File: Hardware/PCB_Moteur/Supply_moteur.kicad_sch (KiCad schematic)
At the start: 26 parts, among them J1 XT30PW-F, U1 L6981N33DR

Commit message: wip: arrangement connecteurs et modeles 3D
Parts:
- L2: DigiKey_Part_Number (none) -> 732-2196-1-ND
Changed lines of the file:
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@@
 			)
 		)
-		(property "Datasheet" ""
+		(property "Datasheet" "https://www.we-online.com/components/products/datasheet/7447715330.pdf"
 			(at 106.68 81.28 0)
 			(effects
@@
 			(at 106.68 81.28 0)
 			(effects
+				(font
+					(size 1.27 1.27)
+				)
+				(hide yes)
+			)
+		)
+		(property "DigiKey_Part_Number" "732-2196-1-ND"
+			(at 106.68 81.28 0)
+			(effects

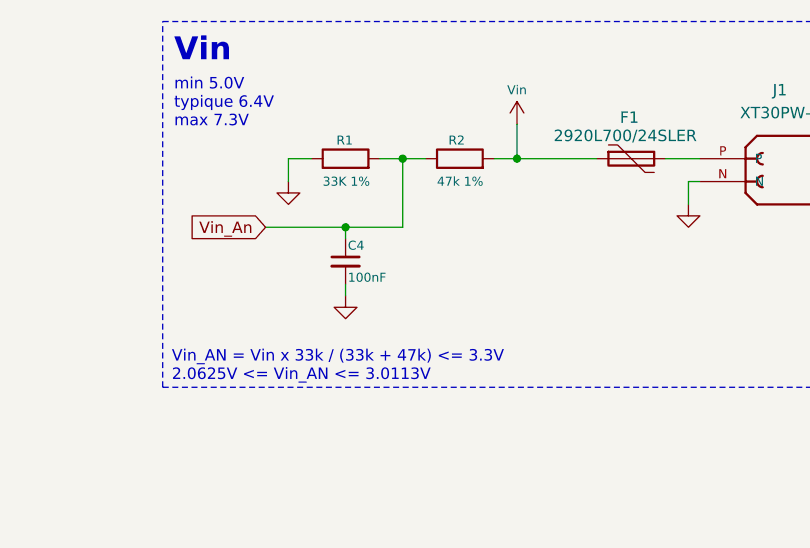
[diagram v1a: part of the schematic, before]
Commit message: fix(GSE & Moteur): change Vin adc divider
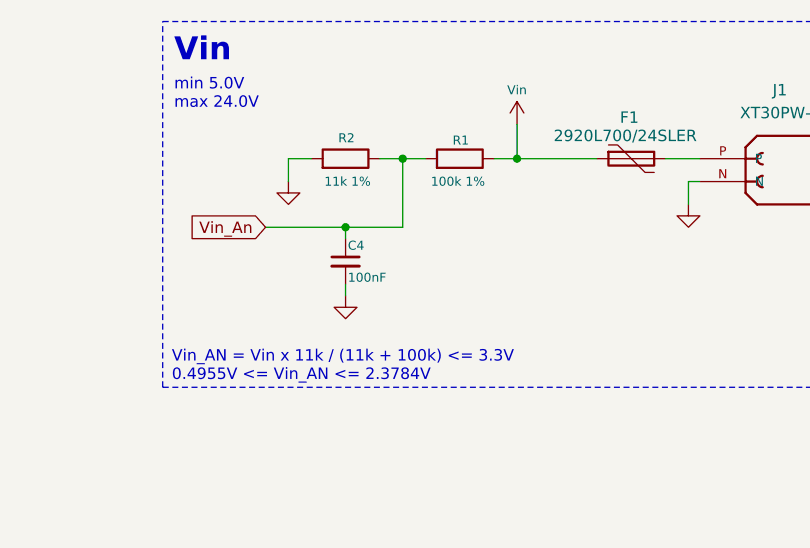
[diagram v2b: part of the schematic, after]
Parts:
- R1: value 33K 1% -> 100k 1%
- R2: value 47k 1% -> 11k 1%
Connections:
- net GND: now also R2.2; no longer R1.1
- net Vin: now also R1.1; no longer R2.2
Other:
- note added: "Vin_AN = Vin x 11k / (11k + 100k) <= 3.3V 0.4955V <= Vin_AN <= 2.3784V"
- note added: "min 5.0V max 24.0V"
- note removed: "Vin_AN = Vin x 33k / (33k + 47k) <= 3.3V 2.0625V <= Vin_AN <= 3.0113V"
- note removed: "min 5.0V typique 6.4V max 7.3V"
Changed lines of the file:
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@@
 		)
 	)
-	(text "Vin_AN = Vin x 33k / (33k + 47k) <= 3.3V\n2.0625V <= Vin_AN <= 3.0113V"
+	(text "Vin_AN = Vin x 11k / (11k + 100k) <= 3.3V\n0.4955V <= Vin_AN <= 2.3784V"
 		(exclude_from_sim no)
 		(at 208.026 51.054 0)
@@
 		)
 	)
-	(text "min 5.0V\ntypique 6.4V\nmax 7.3V"
+	(text "min 5.0V\nmax 24.0V"
 		(exclude_from_sim no)
 		(at 208.28 19.05 0)
@@
 	)
 	(symbol
+		(lib_id "Device:R")
+		(at 227.33 27.94 270)
+		(mirror x)
+		(unit 1)
+		(exclude_from_sim no)
+		(in_bom yes)
+		(on_board yes)
+		(dnp no)
+		(property "Reference" "R2"
+			(at 228.346 25.654 90)
+			(effects
+				(font
+					(size 1 1)
+				)
+				(justify right)
+			)
+		)
+		(property "Value" "11k 1%"
+			(at 230.124 30.48 90)
+			(effects
+				(font
+					(size 1 1)
+				)
+				(justify right)
+			)
+		)
+		(property "Footprint" "Resistor_SMD:R_0805_2012Metric"
+			(at 227.33 29.718 90)
+			(effects
+				(font
+					(size 1 1)
+				)
+				(hide yes)
+			)
+		)
+		(property "Datasheet" "~"
+			(at 227.33 27.94 0)
+			(effects
+				(font
+					(size 1 1)
+				)
+				(hide yes)
+			)
+		)
+		(property "Description" ""
+			(at 227.33 27.94 0)
+			(effects
+				(font
+					(size 1.27 1.27)
+				)
+				(hide yes)
+			)
+		)
+		(pin "1"
+		)
+		(pin "2"
+		)
+		(instances
+			(project "PCB_moteur"
+				(path "/b0d87684-7b1c-41d8-8358-755aa327573e/92d1df5d-a307-4eea-a65c-ade4cb0ad548"
+					(reference "R2")
+					(unit 1)
+				)
+			)
+		)
+	)
+	(symbol
 		(lib_id "Device:LED")
 		(at 123.19 109.22 180)
@@
 	)
 	(symbol
-		(lib_id "Device:R")
-		(at 227.33 27.94 90)
-		(unit 1)
-		(exclude_from_sim no)
-		(in_bom yes)
-		(on_board yes)
-		(dnp no)
-		(property "Reference" "R1"
-			(at 226.314 25.908 90)
-			(effects
-				(font
-					(size 1 1)
-				)
-				(justify right)
-			)
-		)
-		(property "Value" "33K 1%"
-			(at 224.79 30.48 90)
-			(effects
-				(font
-					(size 1 1)
-				)
-				(justify right)
-			)
-		)
-		(property "Footprint" "Resistor_SMD:R_0805_2012Metric"
-			(at 227.33 29.718 90)
-			(effects
-				(font
-					(size 1 1)
-				)
-				(hide yes)
-			)
-		)
-		(property "Datasheet" "~"
-			(at 227.33 27.94 0)
-			(effects
-				(font
-					(size 1 1)
-				)
-				(hide yes)
-			)
-		)
-		(property "Description" ""
-			(at 227.33 27.94 0)
-			(effects
-				(font
-					(size 1.27 1.27)
-				)
-				(hide yes)
-			)
-		)
-		(pin "1"
-		)
-		(pin "2"
-		)
-		(instances
-			(project "PCB_moteur"
-				(path "/b0d87684-7b1c-41d8-8358-755aa327573e/92d1df5d-a307-4eea-a65c-ade4cb0ad548"
-					(reference "R1")
-					(unit 1)
-				)
-			)
-		)
-	)
-	(symbol
 		(lib_id "Device:C_Small")
 		(at 40.64 115.57 0)
@@
 	)
 	(symbol
-		(lib_id "Device:R")
-		(at 240.03 27.94 90)
-		(unit 1)
-		(exclude_from_sim no)
-		(in_bom yes)
-		(on_board yes)
-		(dnp no)
-		(property "Reference" "R2"
-			(at 238.76 25.908 90)
-			(effects
-				(font
-					(size 1 1)
-				)
-				(justify right)
-			)
-		)
-		(property "Value" "47k 1%"
-			(at 237.49 30.48 90)
-			(effects
-				(font
-					(size 1 1)
-				)
-				(justify right)
-			)
-		)
-		(property "Footprint" "Resistor_SMD:R_0805_2012Metric"
-			(at 240.03 29.718 90)
-			(effects
-				(font
-					(size 1 1)
-				)
-				(hide yes)
-			)
-		)
-		(property "Datasheet" "~"
-			(at 240.03 27.94 0)
-			(effects
-				(font
-					(size 1 1)
-				)
-				(hide yes)
-			)
-		)
-		(property "Description" ""
-			(at 240.03 27.94 0)
-			(effects
-				(font
-					(size 1.27 1.27)
-				)
-				(hide yes)
-			)
-		)
-		(pin "1"
-		)
-		(pin "2"
-		)
-		(instances
-			(project "PCB_moteur"
-				(path "/b0d87684-7b1c-41d8-8358-755aa327573e/92d1df5d-a307-4eea-a65c-ade4cb0ad548"
-					(reference "R2")
-					(unit 1)
-				)
-			)
-		)
-	)
-	(symbol
 		(lib_id "power:GND")
 		(at 220.98 30.48 0)
@@
 					(unit 1)
 				)
+			)
+		)
+	)
+	(symbol
+		(lib_id "Device:R")
+		(at 240.03 27.94 270)
+		(mirror x)
+		(unit 1)
+		(exclude_from_sim no)
+		(in_bom yes)
+		(on_board yes)
+		(dnp no)
+		(property "Reference" "R1"
+			(at 241.046 25.908 90)
+			(effects
+				(font
+					(size 1 1)
+				)
+				(justify right)
+			)
+		)
+		(property "Value" "100k 1%"
+			(at 242.824 30.48 90)
+			(effects
+				(font
+					(size 1 1)
+				)
+				(justify right)
+			)
+		)
+		(property "Footprint" "Resistor_SMD:R_0805_2012Metric"
+			(at 240.03 29.718 90)
+			(effects
+				(font
+					(size 1 1)
+				)
+				(hide yes)
+			)
+		)
+		(property "Datasheet" "~"
+			(at 240.03 27.94 0)
+			(effects
+				(font
+					(size 1 1)
+				)
+				(hide yes)
+			)
+		)
+		(property "Description" ""
+			(at 240.03 27.94 0)
+			(effects
+				(font
+					(size 1.27 1.27)
+				)
+				(hide yes)
+			)
+		)
+		(pin "1"
+		)
+		(pin "2"
+		)
+		(instances
+			(project "PCB_moteur"
+				(path "/b0d87684-7b1c-41d8-8358-755aa327573e/92d1df5d-a307-4eea-a65c-ade4cb0ad548"
+					(reference "R1")
+					(unit 1)
+				)

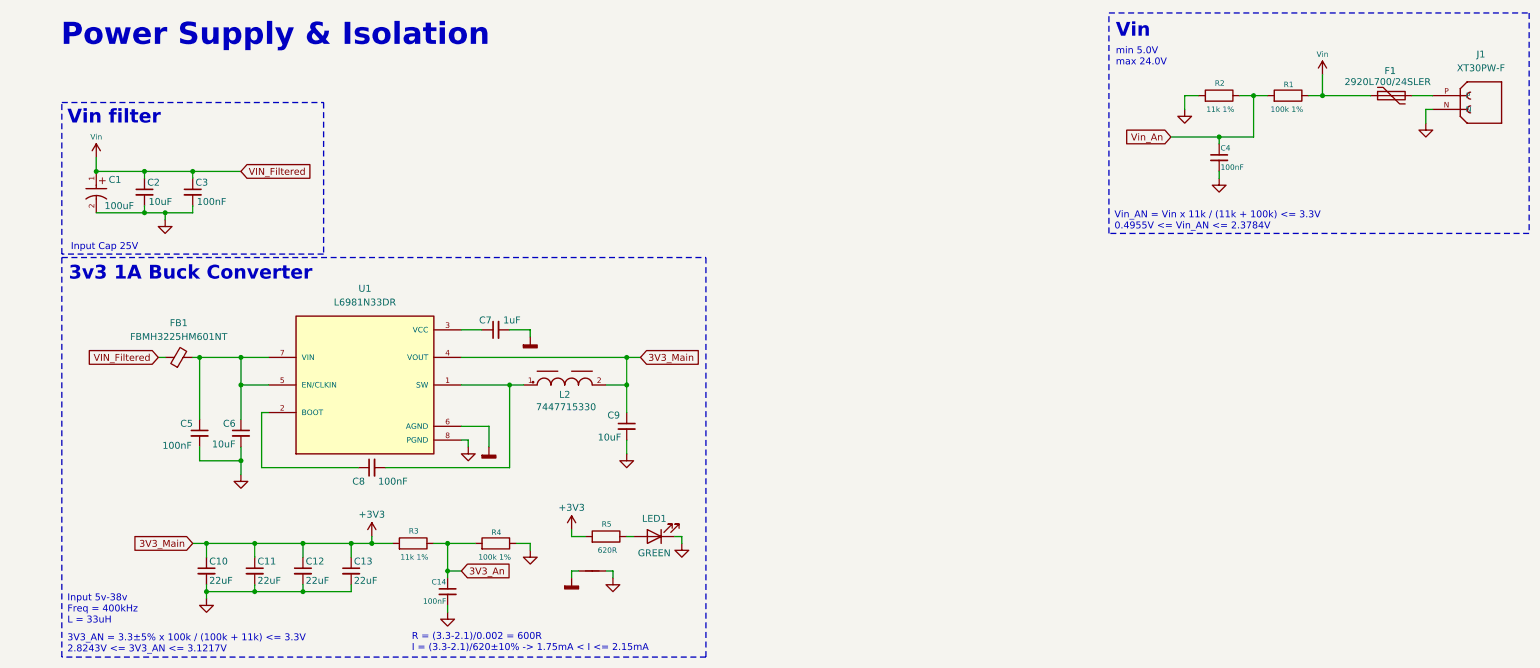
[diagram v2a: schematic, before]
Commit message: wip : work on silkscreen and add all info to BOM
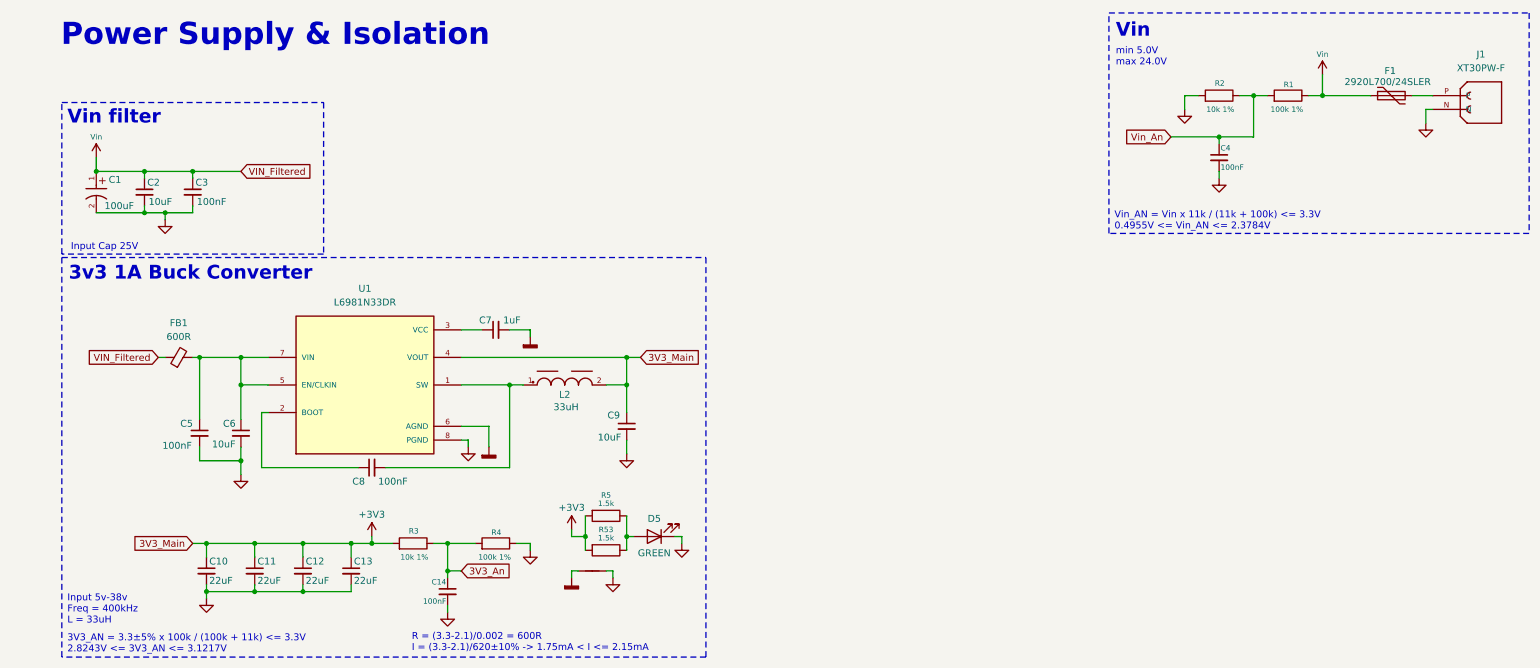
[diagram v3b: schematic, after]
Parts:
- added R53: 1.5k, Resistor_SMD:R_0805_2012Metric, symbol Device:R
- C1: DigiKey_Part_Number (none) -> 732-9215-1-ND; Manufacturer_Part_Number (none) -> 860040573004
- C10, C11, C12, C13: DigiKey_Part_Number (none) -> 445-14428-1-ND; Manufacturer_Part_Number (none) -> C2012X5R1V226M125AC
- C14, C3, C4, C5, C8: DigiKey_Part_Number (none) -> 399-C0805C104K5RACTUCT-ND; Manufacturer_Part_Number (none) -> C0805C104K5RACTU
- C2, C6, C9: DigiKey_Part_Number (none) -> 1276-2891-1-ND; Manufacturer_Part_Number (none) -> CL21A106KAYNNNE
- C7: DigiKey_Part_Number (none) -> 399-C0603C105K4RACTUCT-ND; Manufacturer_Part_Number (none) -> C0603C105K4RACTU
- FB1: value FBMH3225HM601NT -> 600R; DigiKey_Part_Number (none) -> 587-1755-1-ND; Manufacturer_Part_Number (none) -> FBMH3225HM601NT
- J1, NT4: DigiKey_Part_Number (none) -> -; Manufacturer_Part_Number (none) -> -
- L2: value 7447715330 -> 33uH; Manufacturer_Part_Number (none) -> 7447715330
- R1, R4: DigiKey_Part_Number (none) -> 311-100KCRCT-ND; Manufacturer_Part_Number (none) -> RC0805FR-07100KL
- R2, R3: value 11k 1% -> 10k 1%; DigiKey_Part_Number (none) -> 541-10.0KCCT-ND; Manufacturer_Part_Number (none) -> CRCW080510K0FKEA
- R5: value 620R -> 1.5k; DigiKey_Part_Number (none) -> P1.5KDBCT-ND; Manufacturer_Part_Number (none) -> ERA-3AEB152V
- U1: DigiKey_Part_Number (none) -> 497-L6981N33DRCT-ND; Manufacturer_Part_Number (none) -> L6981N33DR
- renumbered LED1 to D5
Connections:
- net +3V3: now also R53.2
- net at D5.2 (A), R5.1: now also R53.1
